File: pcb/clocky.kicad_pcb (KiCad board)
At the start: 2 copper layers, 0 parts

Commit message: Added crystal, fixed footprints, started PCB at 1.4x1.2cm
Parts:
- added C1: C, SM0402, F.Cu at (193.4, 154.3)
- added C2: C, SM0402, F.Cu at (190.0, 153.1)
- added C3: 0.1u, SM0402, F.Cu at (190.6, 161.4)
- added C4: GRM188R60J106ME47D, SM0603, F.Cu at (195.7, 154.0)
- added J1: CONN_5, SIL-5, F.Cu at (198.4, 157.0)
- added J2: CONN_2, SIL-2, F.Cu at (187.6, 163.3)
- added J3: CONN_2, SIL-2, F.Cu at (194.2, 163.3)
- added L1: MLZ2012N4R7LT000, SM0805, F.Cu at (187.8, 160.6)
- added R1: R, SM0402, F.Cu at (188.2, 154.4)
- added R2: R, SM0402, F.Cu at (188.2, 153.4)
- added U1: PIC16LF1709_QFN20, PIC_QFN20, F.Cu at (192.5, 158.0)
- added U2: TLV61220, TLV61220_TSOT23, F.Cu at (187.7, 157.2)
- added U3: NC7WV16L6X, NC7WV16_MICROPAK, F.Cu at (195.6, 160.7)
- added X1: SC20S-12.5PF20PPM, SC-20S, F.Cu at (190.9, 154.4)

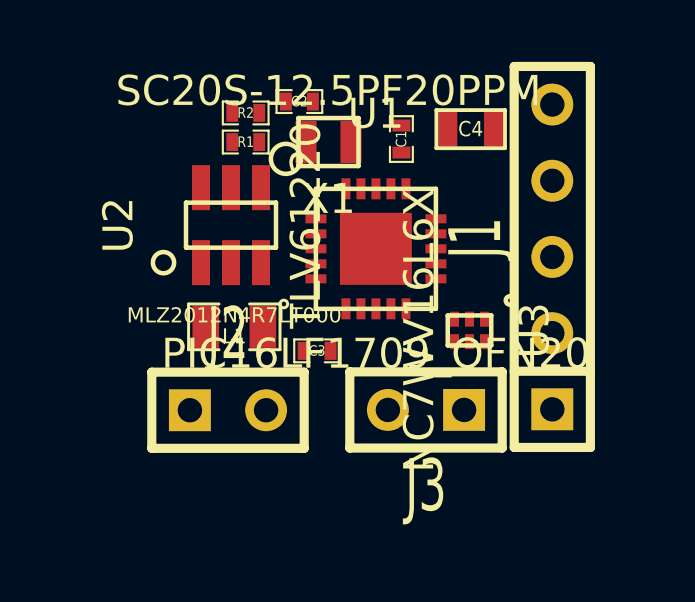
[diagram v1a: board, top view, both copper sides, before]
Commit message: Added some extra pads to expose more micro pins, selectable power supply
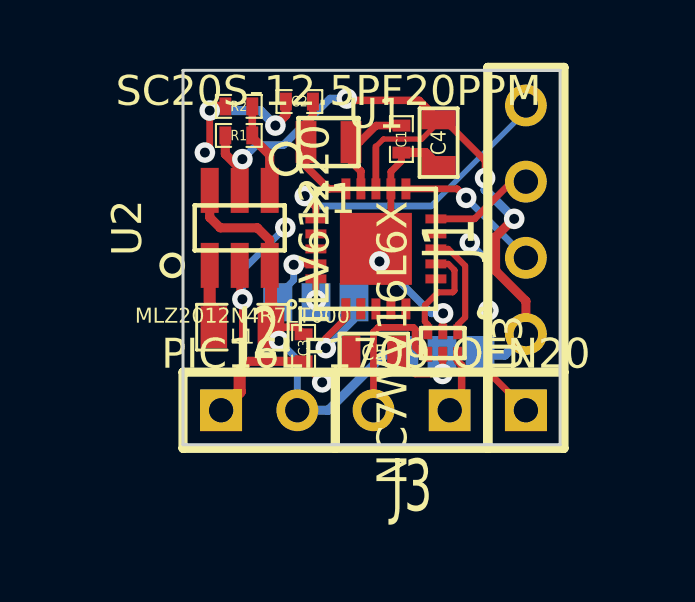
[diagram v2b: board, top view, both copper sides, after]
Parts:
- added C5: GRM188R60J106ME47D, SM0603, F.Cu at (192.4, 161.4)
- added J4: CONN_3, GS3, B.Cu at (190.5, 159.8)
- added SB1: GS3, GS3, B.Cu at (194.7, 161.5)
- moved C4 1.16 mm to (194.6, 154.4), turned to 270 degrees
- moved J2 1.04 mm to (188.6, 163.3)
- moved U3 0.98 mm to (194.7, 161.1)
- moved J1 0.88 mm to (197.5, 157.0)
- moved J3 0.48 mm to (193.7, 163.3)
- moved C3 0.46 mm to (190.1, 161.3), turned to 270 degrees
- moved R1 0.32 mm to (187.9, 154.2)
- moved R2 0.32 mm to (187.9, 153.2)
- moved U2 0.30 mm to (188.0, 157.3)
- moved L1 0.27 mm to (188.1, 160.6)
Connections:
- U1 pad 4: (no net) -> N-0000015
- U1 pad 5: (no net) -> N-0000014
- U1 pad 6: (no net) -> N-0000013
- U3 pad VDD: /VBATT -> N-0000011
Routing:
- net GND: track 0.00 -> 32.0 mm, vias 0 -> 10
- net VDD: track 0.00 -> 25.5 mm, vias 0 -> 4
- net /VBATT: track 0.00 -> 14.8 mm, vias 0 -> 1
- net /~MCLR: track 0.00 -> 9.92 mm, vias 0 -> 1
- net N-000002: track 0.00 -> 5.20 mm
- net /PGD: track 0.00 -> 4.96 mm, vias 0 -> 1
- net N-000003: track 0.00 -> 3.90 mm
- net N-000001: track 0.00 -> 3.60 mm
- net /PGC: track 0.00 -> 3.51 mm
- net N-0000017: track 0.00 -> 3.51 mm
- net N-0000013: track 0.00 -> 3.51 mm, vias 0 -> 1
- net N-000005: track 0.00 -> 3.50 mm
- net N-0000011: track 0.00 -> 3.17 mm, vias 0 -> 1
- net N-0000016: track 0.00 -> 3.04 mm
- net N-0000015: track 0.00 -> 2.22 mm, vias 0 -> 1
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- added copper zone on B.Cu, net GND
- added copper zone on F.Cu, net GND
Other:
- board outline added: 12.6 x 12.5 mm
- net class Default: clearance 0.254 -> 0.1524; trace_width 0.254 -> 0.1524
- rule trace_clearance: 0.254 -> 0.1524
- rule trace_min: 0.254 -> 0.1524
- rule via_min_drill: 0.508 -> 0.3302
- rule via_min_size: 0.889 -> 0.6858
- board text added: "BRN"
